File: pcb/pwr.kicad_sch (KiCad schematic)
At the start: 40 parts, among them J301 USB_C_Receptacle_USB2.0_16P, Q301 Q_Dual_PMOS_S1G1S2G2D2D2D1D1, U301 CYPD3176, U401 AP63205WU, U411 AP63203WU

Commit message: Add title and revision to schematic and board silkscreen, do a bit of tidying of the schematics
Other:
- title: (none) -> ${TITLE}
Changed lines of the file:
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@@
 	(generator_version "9.0")
 	(paper "A4")
+	(title_block
+		(title "${TITLE}")
+		(rev "${REV}")
+	)
 	(rectangle
 		(start 15.24 15.24)

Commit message: Add ESP32, finish wiring. Rev A complete
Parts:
- added D301: VBUS_{C}, LED_SMD:LED_0805_2012Metric_Pad1.15x1.40mm_HandSolder, symbol Device:LED
- added D309: VBUS, LED_SMD:LED_0805_2012Metric_Pad1.15x1.40mm_HandSolder, symbol Device:LED
- added D401: +5V, LED_SMD:LED_0805_2012Metric_Pad1.15x1.40mm_HandSolder, symbol Device:LED
- added D411, D412: D_Schottky, Diode_SMD:D_SOD-123, symbol Device:D_Schottky
- added D413: +3V3, LED_SMD:LED_0805_2012Metric_Pad1.15x1.40mm_HandSolder, symbol Device:LED
- added R301, R401: 5.1k, Resistor_SMD:R_0805_2012Metric_Pad1.20x1.40mm_HandSolder, symbol Device:R
- added R312: 10k, Resistor_SMD:R_0805_2012Metric_Pad1.20x1.40mm_HandSolder, symbol Device:R
- added R411: 1.5k, Resistor_SMD:R_0805_2012Metric_Pad1.20x1.40mm_HandSolder, symbol Device:R
- added TP301: V_{BUS}, TestPoint:TestPoint_Pad_D1.0mm, symbol Connector:TestPoint
- added TP401: +5V, TestPoint:TestPoint_Pad_D1.0mm, symbol Connector:TestPoint
- added TP402: GND, TestPoint:TestPoint_THTPad_D1.0mm_Drill0.5mm, symbol Connector:TestPoint
- added TP411: +3V3, TestPoint:TestPoint_Pad_D1.0mm, symbol Connector:TestPoint
- Q301: MFG Part No (none) -> DMP3085LSD-13
- U301: MFG Part No (none) -> CYPD3176-24LQXQ
- U401: MFG Part No (none) -> AP63205WU-7
- U411: MFG Part No (none) -> AP63203WU-7
- renumbered C302 to C301, C301 to C302, C306 to C303, C305 to C304, C304 to C305, C307 to C306, C303 to C307, D301 to D302, D302 to D303, D303 to D304, D304 to D306, D306 to D307, D307 to D308, R308 to R302, R305 to R303, R306 to R304, R309 to R305, R310 to R306, R303 to R307, R304 to R308, R301 to R309, R302 to R310, R307 to R313
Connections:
- net +3V3: now also R411.2, TP411.1
- net +5V: now also R401.1, TP401.1
- net GND: now also D301.1 (K), D309.1 (K), D401.1 (K), D413.1 (K), TP402.1
- net VBUS_{C}: now also R301.1
- net V_{BUS}: now also D411.2 (A), R312.2, TP301.1; no longer C411.1, U411.2 (EN), U411.3 (IN)
- net D+ renamed USB_{D+}
- net D- renamed USB_{D-}
- new net: D413.2 (A), R411.1
- new net: C411.1, D411.1 (K), D412.1 (K), U411.2 (EN), U411.3 (IN)
- new net: D301.2 (A), R301.2
- new net: D401.2 (A), R401.2
- new net: D309.2 (A), R312.1
- new net VCC_{UART}: D412.2 (A)
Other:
- moved on the sheet: C401, C402, C403, C404, C411, C412, C413, C414, L401, L411, U401, U411

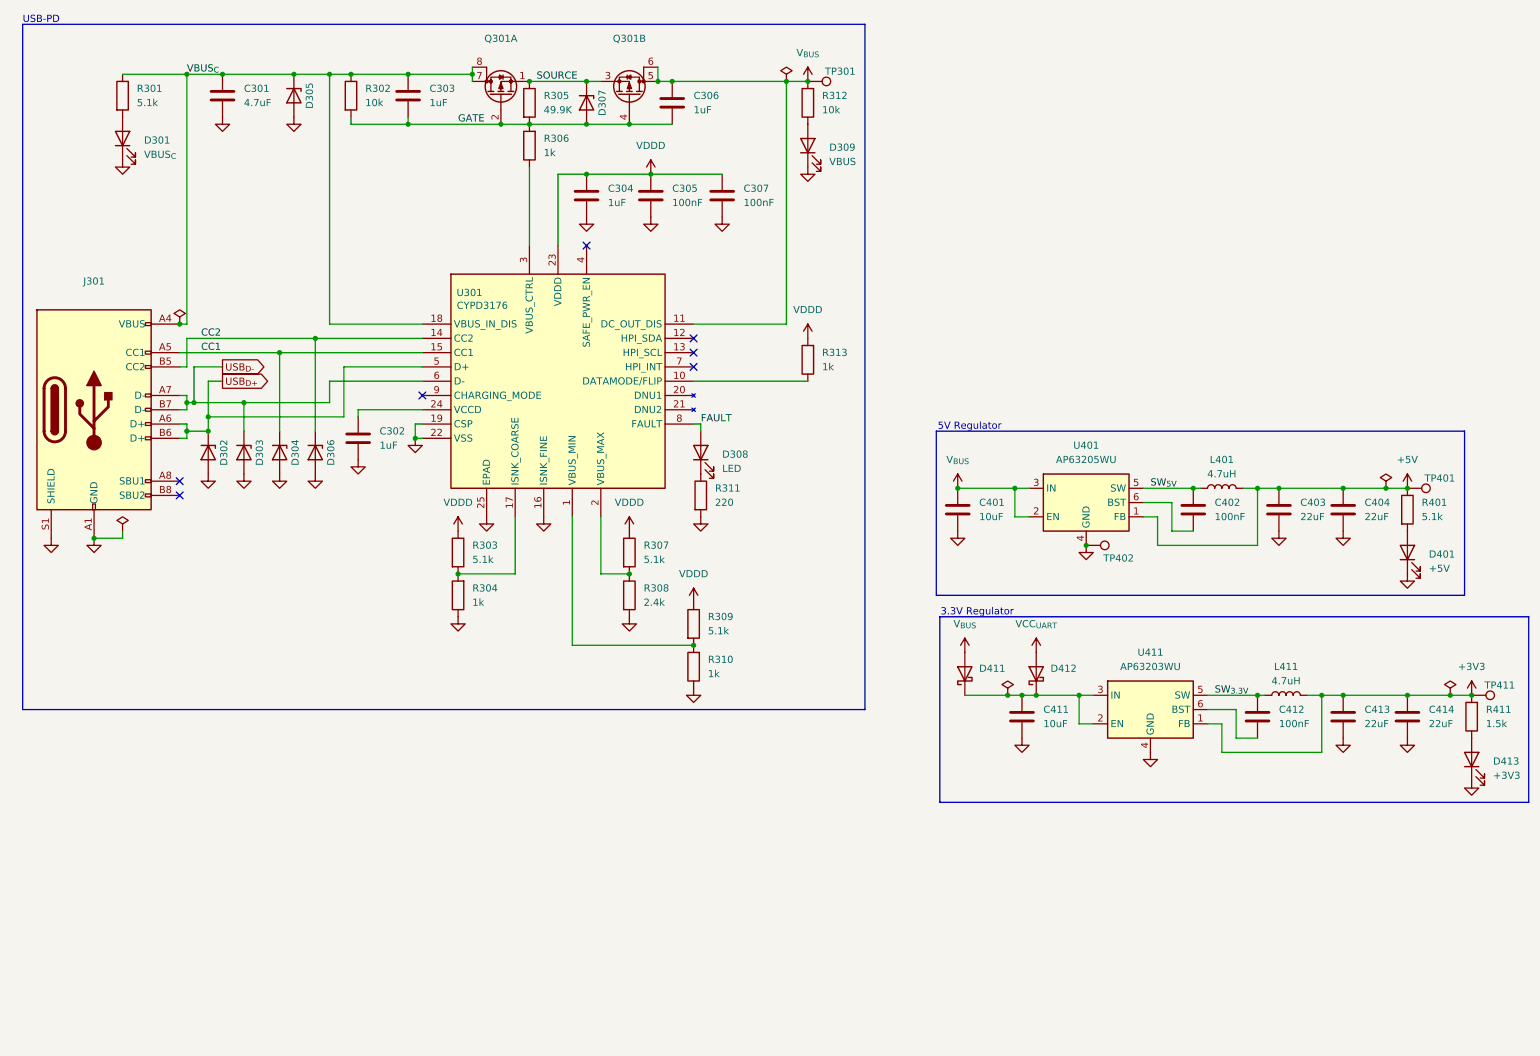
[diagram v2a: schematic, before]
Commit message: Partial Rev B, committing before splitting projects
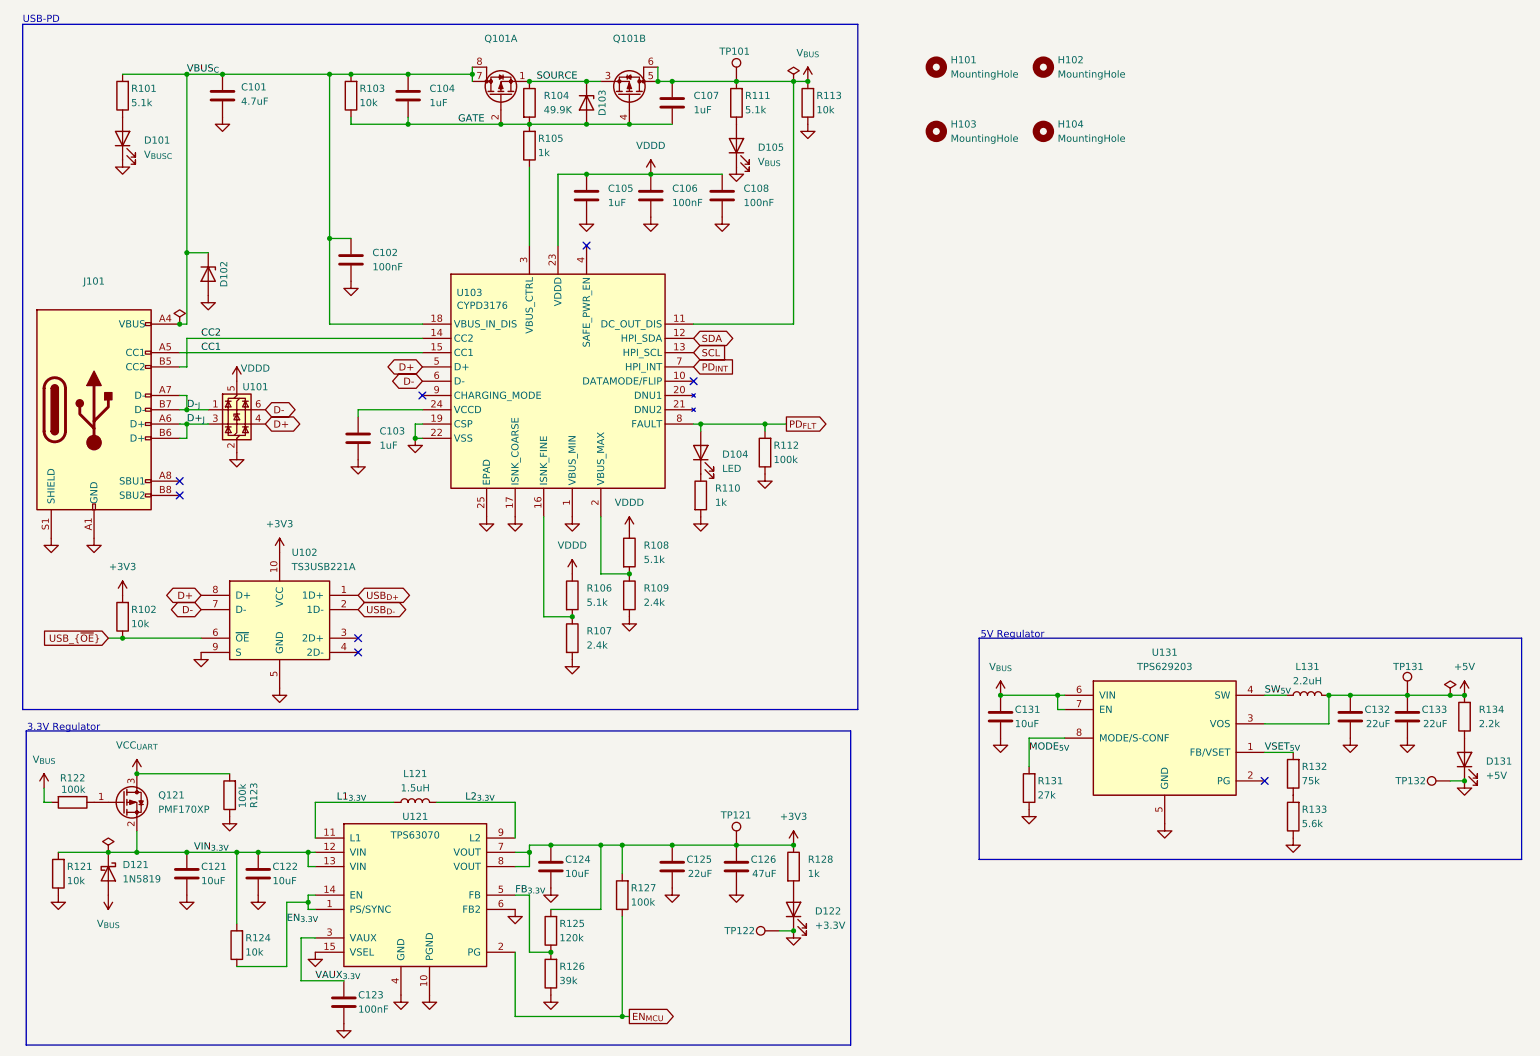
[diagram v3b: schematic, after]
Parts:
- removed C302, C303, C306: 1uF, Capacitor_SMD:C_0805_2012Metric_Pad1.18x1.45mm_HandSolder, symbol Device:C
- removed C307, C402, C412: 100nF, Capacitor_SMD:C_0805_2012Metric_Pad1.18x1.45mm_HandSolder, symbol Device:C
- removed C401, C411: 10uF, Capacitor_SMD:C_0805_2012Metric_Pad1.18x1.45mm_HandSolder, symbol Device:C
- removed C403, C404, C413, C414: 22uF, Capacitor_SMD:C_0805_2012Metric_Pad1.18x1.45mm_HandSolder, symbol Device:C
- removed D301: VBUS_{C}, LED_SMD:LED_0805_2012Metric_Pad1.15x1.40mm_HandSolder, symbol Device:LED
- removed D302, D303: ESDA051, Diode_SMD:D_SOD-323_HandSoldering, symbol Device:D_Zener
- removed D304, D306: ESDA051-1JY, Diode_SMD:D_SOD-323_HandSoldering, symbol Device:D_Zener
- removed D309: VBUS, LED_SMD:LED_0805_2012Metric_Pad1.15x1.40mm_HandSolder, symbol Device:LED
- removed D401: +5V, LED_SMD:LED_0805_2012Metric_Pad1.15x1.40mm_HandSolder, symbol Device:LED
- removed D411, D412: D_Schottky, Diode_SMD:D_SOD-123, symbol Device:D_Schottky
- removed D413: +3V3, LED_SMD:LED_0805_2012Metric_Pad1.15x1.40mm_HandSolder, symbol Device:LED
- removed L401, L411: 4.7uH, Inductor_SMD:L_APV_ANR6045, symbol Device:L
- removed R301, R303, R307, R309, R401: 5.1k, Resistor_SMD:R_0805_2012Metric_Pad1.20x1.40mm_HandSolder, symbol Device:R
- removed R302, R312: 10k, Resistor_SMD:R_0805_2012Metric_Pad1.20x1.40mm_HandSolder, symbol Device:R
- removed R304, R306, R310, R313: 1k, Resistor_SMD:R_0805_2012Metric_Pad1.20x1.40mm_HandSolder, symbol Device:R
- removed R411: 1.5k, Resistor_SMD:R_0805_2012Metric_Pad1.20x1.40mm_HandSolder, symbol Device:R
- removed TP401: +5V, TestPoint:TestPoint_Pad_D1.0mm, symbol Connector:TestPoint
- removed TP402: GND, TestPoint:TestPoint_THTPad_D1.0mm_Drill0.5mm, symbol Connector:TestPoint
- removed TP411: +3V3, TestPoint:TestPoint_Pad_D1.0mm, symbol Connector:TestPoint
- removed U401: AP63205WU, Package_TO_SOT_SMD:TSOT-23-6, symbol Regulator_Switching:AP63205WU
- removed U411: AP63203WU, Package_TO_SOT_SMD:TSOT-23-6, symbol Regulator_Switching:AP63203WU
- added C102, C108, C123: 100nF, Capacitor_SMD:C_0402_1005Metric, symbol Device:C
- added C103, C104, C107: 1uF, Capacitor_SMD:C_0402_1005Metric, symbol Device:C
- added C121, C131: 10uF, Capacitor_SMD:C_0805_2012Metric, symbol Device:C
- added C122, C124: 10uF, Capacitor_SMD:C_0603_1608Metric, symbol Device:C
- added C125, C132, C133: 22uF, Capacitor_SMD:C_1206_3216Metric, symbol Device:C
- added C126: 47uF, Capacitor_SMD:C_1206_3216Metric, symbol Device:C
- added D101: V_{BUSC}, LED_SMD:LED_0603_1608Metric, symbol Device:LED
- added D105: V_{BUS}, LED_SMD:LED_0603_1608Metric, symbol Device:LED
- added D121: 1N5819, Diode_SMD:D_SOD-123, symbol Device:D_Schottky
- added D122: +3.3V, LED_SMD:LED_0603_1608Metric, symbol Device:LED
- added D131: +5V, LED_SMD:LED_0603_1608Metric, symbol Device:LED
- added H101, H102, H103, H104: MountingHole, MountingHole:MountingHole_3.2mm_M3_ISO7380, symbol Mechanical:MountingHole
- added L121: 1.5uH, nixie_clock:L_Bourns_SRN5040TA, symbol Device:L
- added L131: 2.2uH, nixie_clock:L_Bourns_SRN5040TA, symbol Device:L
- added Q121: PMF170XP, Package_TO_SOT_SMD:SOT-323_SC-70, symbol Transistor_FET:Q_PMOS_GSD
- added R101, R111: 5.1k, Resistor_SMD:R_0603_1608Metric, symbol Device:R
- added R102, R103, R113, R121, R124: 10k, Resistor_SMD:R_0402_1005Metric, symbol Device:R
- added R105, R128: 1k, Resistor_SMD:R_0402_1005Metric, symbol Device:R
- added R106, R108: 5.1k, Resistor_SMD:R_0402_1005Metric, symbol Device:R
- added R107: 2.4k, Resistor_SMD:R_0402_1005Metric, symbol Device:R
- added R112, R122, R123, R127: 100k, Resistor_SMD:R_0402_1005Metric, symbol Device:R
- added R125: 120k, Resistor_SMD:R_0402_1005Metric, symbol Device:R
- added R126: 39k, Resistor_SMD:R_0402_1005Metric, symbol Device:R
- added R131: 27k, Resistor_SMD:R_0402_1005Metric, symbol Device:R
- added R132: 75k, Resistor_SMD:R_0402_1005Metric, symbol Device:R
- added R133: 5.6k, Resistor_SMD:R_0402_1005Metric, symbol Device:R
- added R134: 2.2k, Resistor_SMD:R_0402_1005Metric, symbol Device:R
- added TP121: +3V3, TestPoint:TestPoint_Pad_D1.0mm, symbol Connector:TestPoint
- added TP122, TP132: GND, TestPoint:TestPoint_Pad_D1.0mm, symbol Connector:TestPoint
- added TP131: +5V, TestPoint:TestPoint_Pad_D1.0mm, symbol Connector:TestPoint
- added U101: USBLC6-2SC6, Package_TO_SOT_SMD:SOT-23-6, symbol Power_Protection:USBLC6-2SC6
- added U102: TS3USB221A, nixie_clock:UQFN-10_1.5x2mm_P0.5mm_TI_RSE0010A, symbol nixie_clock:TS3USB221A
- added U121: TPS63070, nixie_clock:VQFN-15_2.5x3mm_TI_RNM0015A, symbol nixie_clock:TPS63070
- added U131: TPS629203, Package_TO_SOT_SMD:SOT-583-8, symbol nixie_clock:TPS629203
- C101: renamed from C301; LCSC (none) -> C1779; MFG Part No C0805C475K3RACTU -> CL21A475KAQNNNE
- C105: renamed from C304; footprint Capacitor_SMD:C_0805_2012Metric_Pad1.18x1.45mm_HandSolder -> Capacitor_SMD:C_0402_1005Metric; LCSC (none) -> C52923; MFG Part No C0805C105K3RACTU -> CL05A105KA5NQNC
- C106: renamed from C305; footprint Capacitor_SMD:C_0805_2012Metric_Pad1.18x1.45mm_HandSolder -> Capacitor_SMD:C_0402_1005Metric; LCSC (none) -> C1525; MFG Part No C0805C104K3RACTU -> CL05B104KO5NNNC
- D102: renamed from D305; value SMAJ15A -> SD15Q-7; footprint Diode_SMD:D_SMA_Handsoldering -> Diode_SMD:D_SOD-323; LCSC (none) -> C19950473; MFG Part No SMAJ15A -> SD15Q-7
- D104: renamed from D308; footprint LED_SMD:LED_1206_3216Metric_Pad1.42x1.75mm_HandSolder -> LED_SMD:LED_0603_1608Metric; LCSC (none) -> C2286; MFG Part No CMD15-21VRD/TR8 -> KT-0603R
- R104: renamed from R305; footprint Resistor_SMD:R_0805_2012Metric_Pad1.20x1.40mm_HandSolder -> Resistor_SMD:R_0402_1005Metric; LCSC (none) -> C25897; MFG Part No RMCF0805FT49K9 -> 0402WGF4992TCE
- R109: renamed from R308; footprint Resistor_SMD:R_0805_2012Metric_Pad1.20x1.40mm_HandSolder -> Resistor_SMD:R_0402_1005Metric; LCSC (none) -> C25905; MFG Part No RMCF0805FT2K40 -> 0402WGF5101TCE
- R110: renamed from R311; value 220 -> 1k; footprint Resistor_SMD:R_0805_2012Metric_Pad1.20x1.40mm_HandSolder -> Resistor_SMD:R_0402_1005Metric; LCSC (none) -> C11702; MFG Part No RMCF0805FT220R -> 0402WGF1001TCE
- renumbered D307 to D103, J301 to J101, Q301 to Q101, TP301 to TP101, U301 to U103
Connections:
- net +3V3: now also C124.1, C125.1, C126.1, R102.2, R125.2, R127.2, R128.1, TP121.1, U102.10 (VCC), U121.7 (VOUT), U121.8 (VOUT)
- net +5V: now also C132.1, C133.1, L131.2, R134.2, TP131.1, U131.3 (VOS)
- net GATE: now also C104.2, C107.2, R103.1, R105.2
- net GND: now also U103.1 (VBUS_MIN), U103.17 (ISNK_COARSE), C102.2, C103.2, C108.2, C121.2, C122.2, C123.2, C124.2, C125.2, C126.2, C131.2, C132.2, C133.2, D101.1 (K), D105.1 (K), D122.1 (K), D131.1 (K), R107.2, R112.1, R113.1, R121.1, R123.1, R126.1, R131.1, R133.1, TP122.1, TP132.1, U101.2 (GND), U102.5 (GND), U102.9 (S), U121.10 (PGND), U121.15 (VSEL), U121.4 (GND), U121.6 (FB2), U131.5 (GND); no longer U103.16 (ISNK_FINE)
- net SW_{5V}: now also L131.1, U131.4 (SW)
- net USB_{D+}: now also U102.1 (1D+); no longer J101.A6 (D+), J101.B6 (D+), U103.5 (D+)
- net USB_{D-}: now also U102.2 (1D-); no longer J101.A7 (D-), J101.B7 (D-), U103.6 (D-)
- net VBUS_{C}: now also C102.1, C104.1, R101.2, R103.2
- net VCC_{UART}: now also Q121.3 (D), R123.2
- net VDDD: now also C108.1, R106.1, R108.1, U101.5 (VBUS)
- net V_{BUS}: now also C107.1, C131.1, D121.2 (A), R111.2, R113.2, R122.2, U131.6 (VIN), U131.7 (EN)
- net SDA: now reaches U103.12 (HPI_SDA)
- net SCL: now reaches U103.13 (HPI_SCL)
- net at R109.1, U103.2 (VBUS_MAX): now also R108.2
- net at U103.24 (VCCD): now also C103.1
- net at U103.3 (VBUS_CTRL): now also R105.1
- net PD_{INT}: now reaches U103.7 (HPI_INT)
- net FAULT renamed PD_{FLT}
- net PD_{FLT}: now also R112.2
- new net: Q121.1 (G), R122.1
- new net: D101.2 (A), R101.1
- new net: R106.2, R107.1, U103.16 (ISNK_FINE)
- new net: R132.1, R133.2
- new net: D122.2 (A), R128.2
- new net: D105.2 (A), R111.1
- new net: D131.2 (A), R134.1
- new net D+: U101.4 (I/O2), U102.8 (D+), U103.5 (D+)
- new net D+_{J}: J101.A6 (D+), J101.B6 (D+), U101.3 (I/O2)
- new net D-: U101.6 (I/O1), U102.7 (D-), U103.6 (D-)
- new net D-_{J}: J101.A7 (D-), J101.B7 (D-), U101.1 (I/O1)
- new net EN_{3.3V}: R124.1, U121.1 (PS/SYNC), U121.14 (EN)
- new net EN_{MCU}: R127.1, U121.2 (PG)
- new net FB_{3.3V}: R125.1, R126.2, U121.5 (FB)
- new net L1_{3.3V}: L121.1, U121.11 (L1)
- new net L2_{3.3V}: L121.2, U121.9 (L2)
- new net MODE_{5V}: R131.2, U131.8 (MODE/S-CONF)
- new net USB_{~{OE}}: R102.1, U102.6 (~{OE})
- new net VAUX_{3.3V}: C123.1, U121.3 (VAUX)
- new net VIN_{3.3V}: C121.1, C122.1, D121.1 (K), Q121.2 (S), R121.2, R124.2, U121.12 (VIN), U121.13 (VIN)
- new net VSET_{5V}: R132.2, U131.1 (FB/VSET)
- no-connect marks 7 -> 8
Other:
- moved on the sheet: D102, TP101
